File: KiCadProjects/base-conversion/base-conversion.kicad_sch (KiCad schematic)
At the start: 13 parts, among them J1 Conn_01x04_Pin, J2 Conn_01x06_Pin, J3 Conn_01x04_Pin, J4 Conn_01x01_Pin, J5 Conn_01x01_Pin, J6 Conn_01x04_Pin, U1 AT28C62256-15PU, U2 AT28C62256-15PU, U3 AT28C62256-15PU, U4 AT28C62256-15PU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

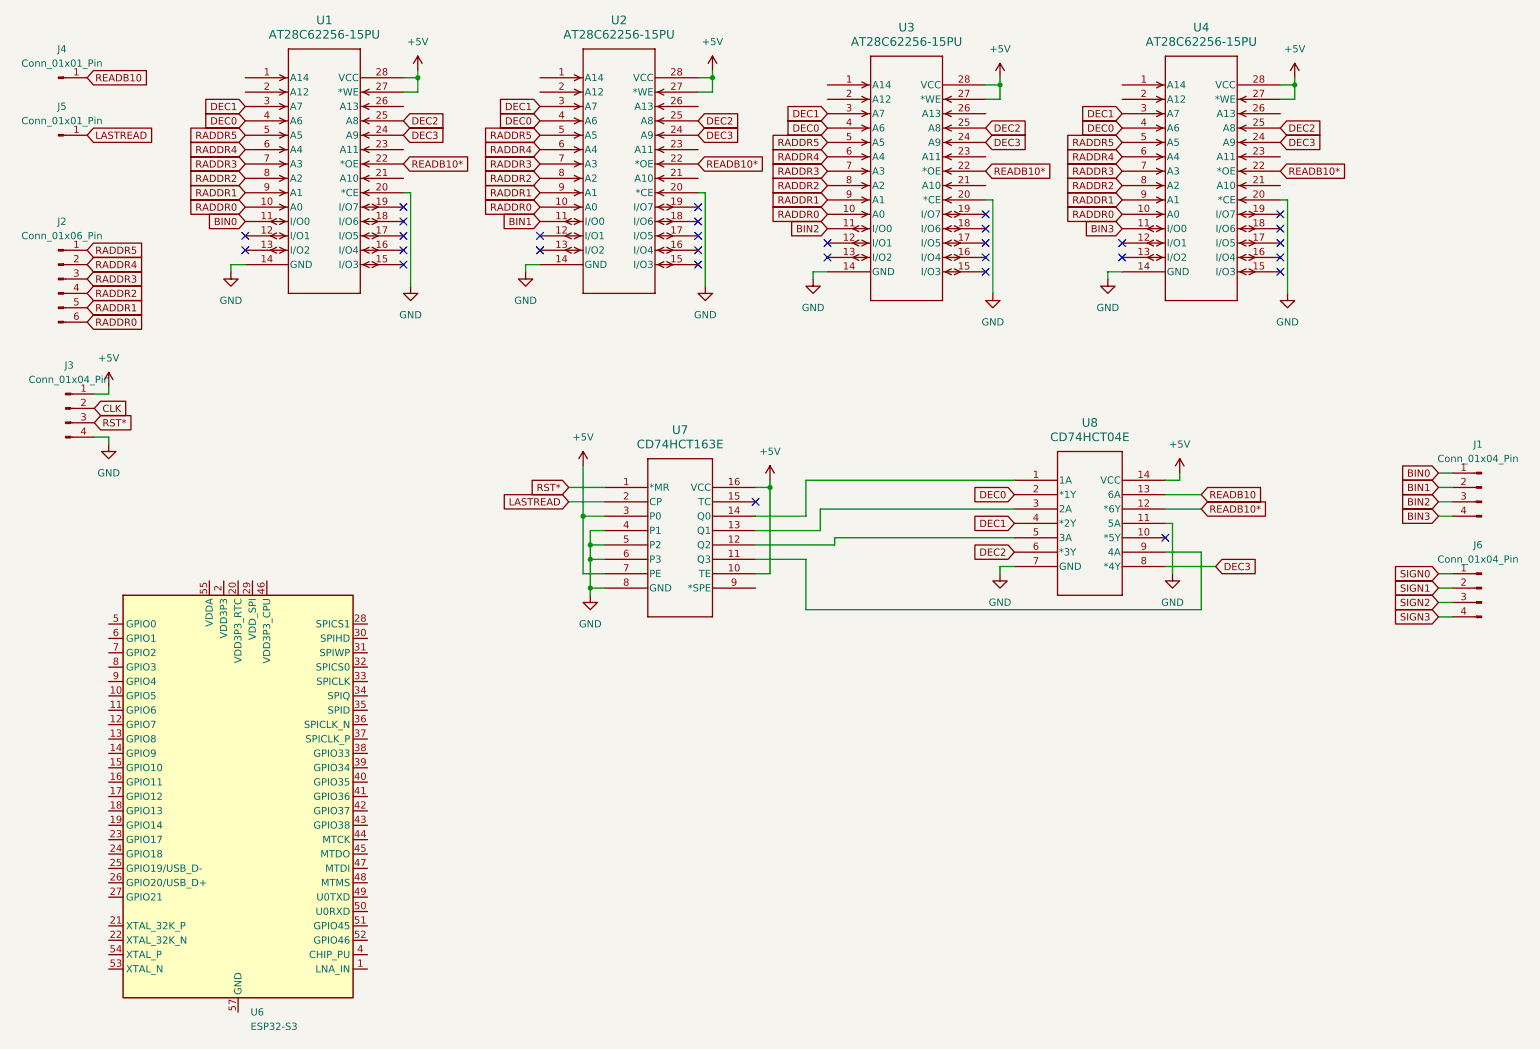
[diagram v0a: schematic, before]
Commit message: Create KiCad schematics based on breadboards
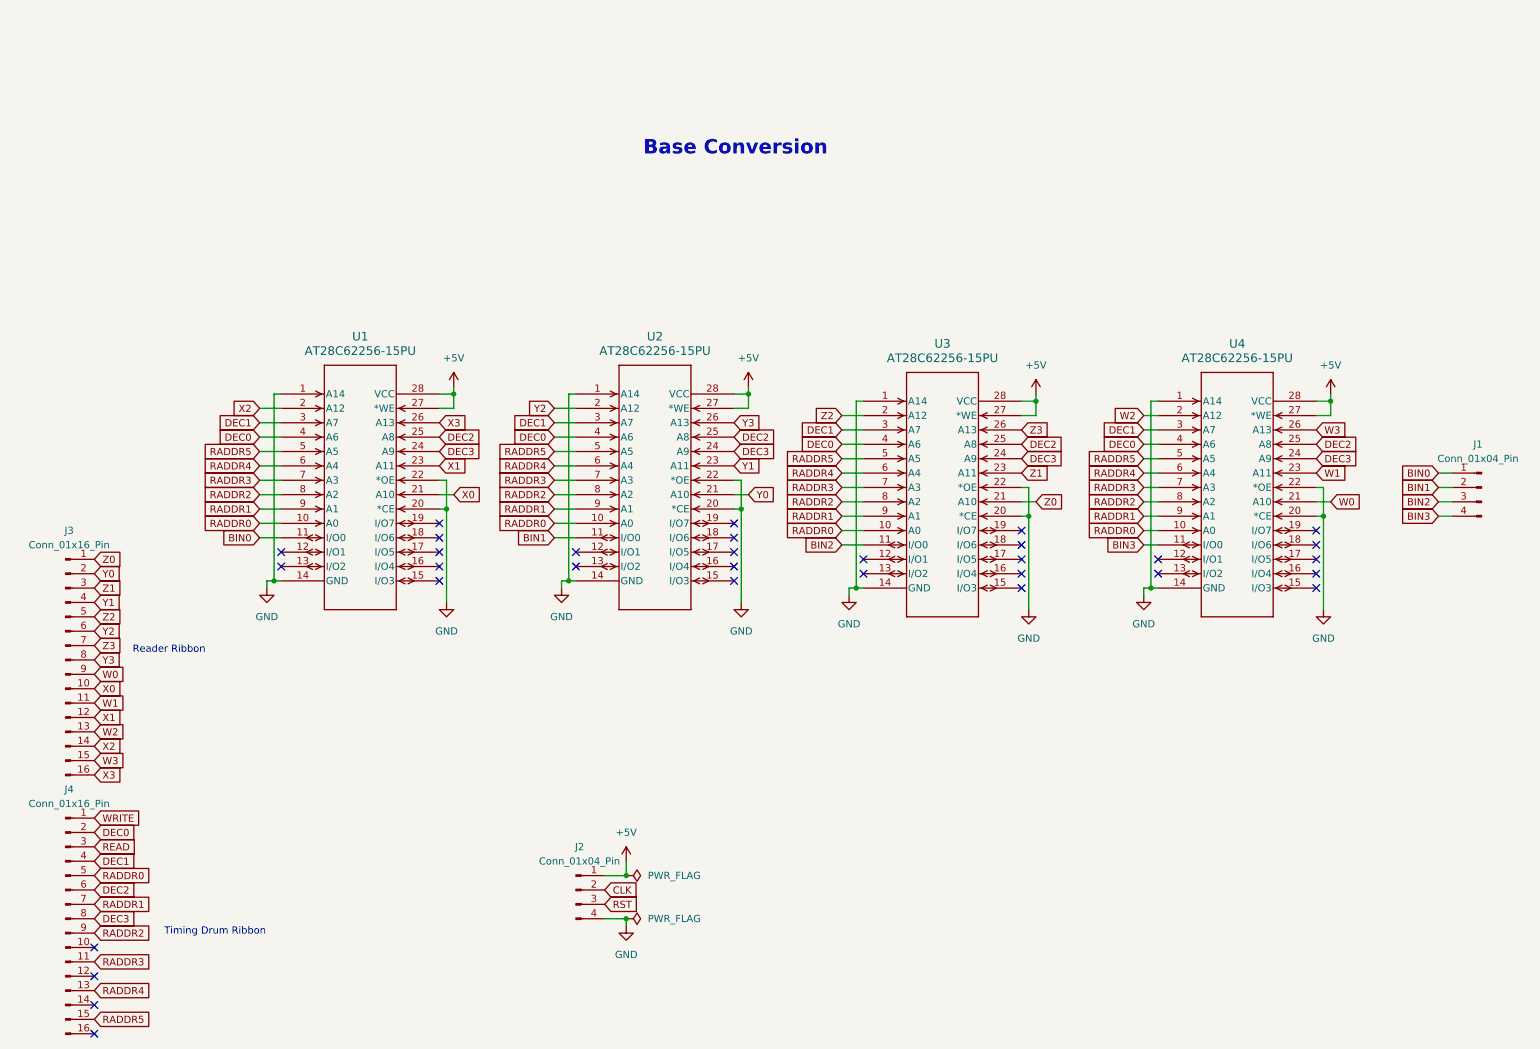
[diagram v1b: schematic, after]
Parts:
- removed J2: Conn_01x06_Pin, symbol Connector:Conn_01x06_Pin
- removed J3, J6: Conn_01x04_Pin, symbol Connector:Conn_01x04_Pin
- removed J4, J5: Conn_01x01_Pin, symbol Connector:Conn_01x01_Pin
- removed U6: ESP32-S3, Package_DFN_QFN:QFN-56-1EP_7x7mm_P0.4mm_EP4x4mm, symbol MCU_Espressif:ESP32-S3
- removed U7: CD74HCT163E, N16, symbol 0_base_conversion:CD74HCT163E
- removed U8: CD74HCT04E, N14, symbol 0_base_conversion:CD74HCT04E
- added J2: Conn_01x04_Pin, Connector_PinHeader_2.54mm:PinHeader_1x04_P2.54mm_Vertical, symbol Connector:Conn_01x04_Pin
- added J3, J4: Conn_01x16_Pin, symbol Connector:Conn_01x16_Pin
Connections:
- net READB10* is gone; now on net GND: U1.22 (*OE), U2.22 (*OE), U3.22 (*OE), U4.22 (*OE)
- net +5V: now also J2.1 (Pin_1)
- net CLK: now also J2.2 (Pin_2)
- net DEC0: now also J4.2 (Pin_2)
- net DEC1: now also J4.4 (Pin_4)
- net DEC2: now also J4.6 (Pin_6)
- net DEC3: now also J4.8 (Pin_8)
- net GND: now also U1.1 (A14), U2.1 (A14), U3.1 (A14), U4.1 (A14), J2.4 (Pin_4)
- net RADDR0: now also J4.5 (Pin_5)
- net RADDR1: now also J4.7 (Pin_7)
- net RADDR2: now also J4.9 (Pin_9)
- net RADDR3: now also J4.11 (Pin_11)
- net RADDR4: now also J4.13 (Pin_13)
- net RADDR5: now also J4.15 (Pin_15)
- net Z2: now reaches U3.2 (A12)
- net Z2: now also J3.5 (Pin_5)
- net Z0: now reaches U3.21 (A10)
- net Z0: now also J3.1 (Pin_1)
- net Z1: now reaches U3.23 (A11)
- net Z1: now also J3.3 (Pin_3)
- net Z3: now reaches U3.26 (A13)
- net Z3: now also J3.7 (Pin_7)
- net W2: now reaches U4.2 (A12)
- net W2: now also J3.13 (Pin_13)
- net W0: now reaches U4.21 (A10)
- net W0: now also J3.9 (Pin_9)
- net W1: now reaches U4.23 (A11)
- net W1: now also J3.11 (Pin_11)
- net W3: now reaches U4.26 (A13)
- net W3: now also J3.15 (Pin_15)
- net X2: now reaches U1.2 (A12)
- net X2: now also J3.14 (Pin_14)
- net X0: now reaches U1.21 (A10)
- net X0: now also J3.10 (Pin_10)
- net X1: now reaches U1.23 (A11)
- net X1: now also J3.12 (Pin_12)
- net X3: now reaches U1.26 (A13)
- net X3: now also J3.16 (Pin_16)
- net Y2: now reaches U2.2 (A12)
- net Y2: now also J3.6 (Pin_6)
- net Y0: now reaches U2.21 (A10)
- net Y0: now also J3.2 (Pin_2)
- net Y1: now reaches U2.23 (A11)
- net Y1: now also J3.4 (Pin_4)
- net Y3: now reaches U2.26 (A13)
- net Y3: now also J3.8 (Pin_8)
- new net READ: J4.3 (Pin_3)
- new net RST: J2.3 (Pin_3)
- new net WRITE: J4.1 (Pin_1)
- no-connect marks 30 -> 32
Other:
- note added: "Base Conversion"
- note added: "Reader Ribbon"
- note added: "Timing Drum Ribbon"
- moved on the sheet: U1, U2, U3, U4
